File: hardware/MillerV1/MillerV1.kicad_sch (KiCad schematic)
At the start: 281 parts, among them IC1 TUSB1106PWR, J2 Conn_02x04_Counter_Clockwise, Q1 Q12MHz/20pF/10ppm/4P/3.2x2.5mm, U1 CCGM1A1(FBGA-324), U10 RP2040(QFN-56_7x7mm_P0.4mm), U11 TPS62A02ADRLR(SOT-563-6), U12 TPS62A02ADRLR(SOT-563-6), U13 TPS62A02ADRLR(SOT-563-6), U14 TPS62A02ADRLR(SOT-563-6), U15 TPS62A02ADRLR(SOT-563-6)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

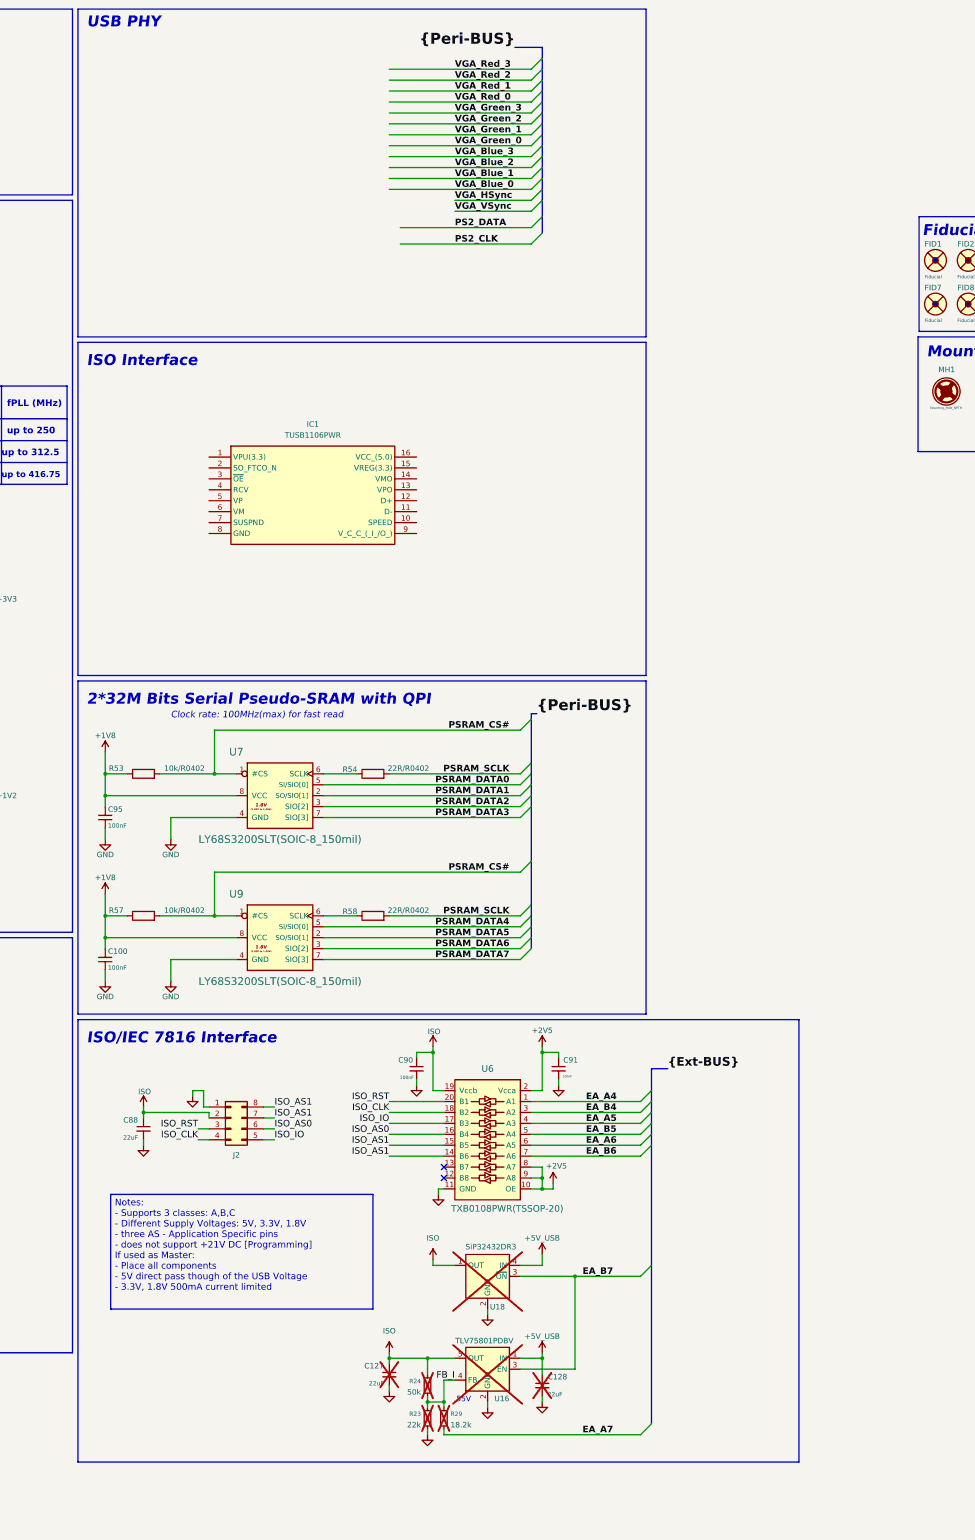
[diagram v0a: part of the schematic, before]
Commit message: merged USB PHY
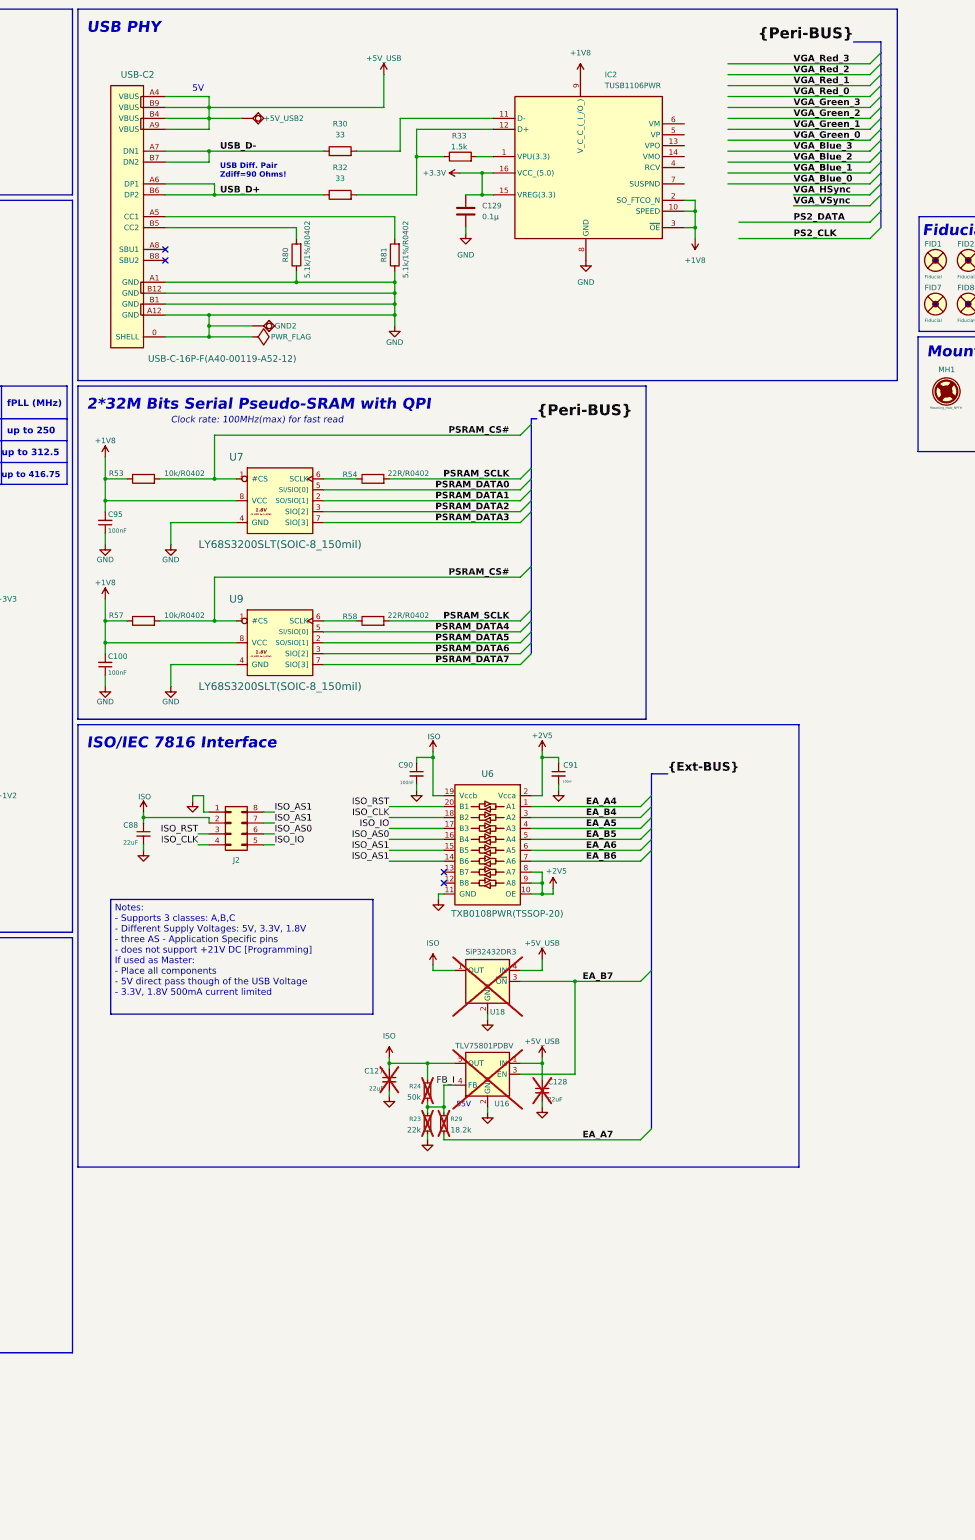
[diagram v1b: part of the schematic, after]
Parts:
- removed IC1: TUSB1106PWR, New_Libary:SOP65P640X120-16N, symbol New_Library:TUSB1106PWR
- added +5V_USB2, GND2: TESTPAD, OLIMEX_Other-FP:TEST_PAD_40x70_Round, symbol OLIMEX_OTHER:TESTPAD
- added C129: 0.1µ, New_Libary:C_0402_5MIL_DWS, symbol Device:C
- added IC2: TUSB1106PWR, New_Libary:SOP65P640X120-16N, symbol New_Library:TUSB1106PWR
- added R30, R32: 33, New_Libary:R_0402_5MIL_DWS, symbol Device:R
- added R33: 1.5k, New_Libary:R_0402_5MIL_DWS, symbol Device:R
- added R80, R81: 5.1k/1%/R0402, OLIMEX_RLC-FP:R_0402_5MIL_DWS, symbol OLIMEX_RCL:R
- added USB-C2: USB-C-16P-F(A40-00119-A52-12), New_Libary:USB2.0_TYPE-C(A40-00119-A52-12)_Paste, symbol OLIMEX_Connectors:USB2.0_TYPE-C(A40-00119-A52-12)
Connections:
- net +1V8: now also IC2.10 (SPEED), IC2.2 (SO_FTCO_N), IC2.3 (~{OE}), IC2.9 (V_C_C_(_I_/O_))
- net +5V_USB: now also +5V_USB2.1 (Pad), USB-C2.A4 (VBUS), USB-C2.A9 (VBUS), USB-C2.B4 (VBUS), USB-C2.B9 (VBUS)
- net GND: now also C129.2, GND2.1 (Pad), IC2.8 (GND), R80.1, R81.1, USB-C2.0 (SHELL), USB-C2.A1 (GND), USB-C2.A12 (GND), USB-C2.B1 (GND), USB-C2.B12 (GND)
- net USB_D+: now also R32.1, USB-C2.A6 (DP1), USB-C2.B6 (DP2)
- net USB_D-: now also R30.1, USB-C2.A7 (DN1), USB-C2.B7 (DN2)
- new net: IC2.12 (D+), R32.2, R33.1
- new net: R81.2, USB-C2.A5 (CC1)
- new net: IC2.1 (VPU(3.3)), R33.2
- new net: IC2.11 (D-), R30.2
- new net: R80.2, USB-C2.B5 (CC2)
- new net +3.3V: C129.1, IC2.15 (VREG(3.3)), IC2.16 (VCC_(5.0))
- no-connect marks 5 -> 7
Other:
- note added: "5V"
- note removed: "ISO Interface"
- moved on the sheet: C100, C127, C128, C88, C90, C91, C95, J2, R23, R24, R29, R53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

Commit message: assigned FPGA pins to USB PHY
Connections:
- net PS2_CLK is gone; now on net SUSPEND: U1.N1 (IO_WB_A0)
- net PS2_DATA is gone; now on net RCV: U1.N2 (IO_WB_B0)
- net VGA_Green_0 is gone; now on net VP: U1.K2 (IO_WB_B5)
- net VGA_Green_1 is gone; now on net VM: U1.K1 (IO_WB_A5)
- net VGA_Red_0 is gone; now on net VMO: U1.L2 (IO_WB_B3)
- net VGA_Red_1 is gone; now on net VPO: U1.L1 (IO_WB_A3)
- net VPO: now reaches IC2.13 (VPO)
- net VMO: now reaches IC2.14 (VMO)
- net RCV: now reaches IC2.4 (RCV)
- net VP: now reaches IC2.5 (VP)
- net VM: now reaches IC2.6 (VM)
- net SUSPEND: now reaches IC2.7 (SUSPND)
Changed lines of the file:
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@@
 	(wire
 		(pts
+			(xy 730.25 52.07) (xy 722.63 52.07)
+		)
+		(stroke
+			(width 0)
+			(type default)
+		)
+	)
+	(wire
+		(pts
 			(xy 588.01 139.7) (xy 588.01 137.16)
 		)
@@
 	(wire
 		(pts
+			(xy 722.63 55.88) (xy 727.71 55.88)
+		)
+		(stroke
+			(width 0)
+			(type default)
+		)
+	)
+	(wire
+		(pts
 			(xy 152.4 292.1) (xy 165.1 292.1)
 		)
@@
 	(wire
 		(pts
+			(xy 723.9 33.02) (xy 723.9 46.99)
+		)
+		(stroke
+			(width 0)
+			(type default)
+		)
+	)
+	(wire
+		(pts
 			(xy 43.18 247.65) (xy 86.36 247.65)
 		)
@@
 	(wire
 		(pts
-			(xy 732.79 35.56) (xy 765.81 35.56)
-		)
-		(stroke
-			(width 0)
-			(type default)
-		)
-	)
-	(wire
-		(pts
 			(xy 439.42 44.45) (xy 436.88 44.45)
 		)
@@
 	(wire
 		(pts
-			(xy 735.33 68.58) (xy 765.81 68.58)
+			(xy 68.58 93.98) (xy 78.74 93.98)
 		)
 		(stroke
@@
 	(wire
 		(pts
-			(xy 68.58 93.98) (xy 78.74 93.98)
+			(xy 154.94 76.2) (xy 167.64 76.2)
 		)
 		(stroke
@@
 	(wire
 		(pts
-			(xy 154.94 76.2) (xy 167.64 76.2)
+			(xy 725.17 35.56) (xy 765.81 35.56)
 		)
 		(stroke
@@
 	(wire
 		(pts
+			(xy 725.17 49.53) (xy 722.63 49.53)
+		)
+		(stroke
+			(width 0)
+			(type default)
+		)
+	)
+	(wire
+		(pts
 			(xy 449.58 251.46) (xy 449.58 254)
 		)
@@
 	(wire
 		(pts
+			(xy 722.63 45.72) (xy 765.81 45.72)
+		)
+		(stroke
+			(width 0)
+			(type default)
+		)
+	)
+	(wire
+		(pts
 			(xy 342.9 147.32) (xy 342.9 152.4)
 		)
@@
 	(wire
 		(pts
+			(xy 730.25 64.77) (xy 765.81 64.77)
+		)
+		(stroke
+			(width 0)
+			(type default)
+		)
+	)
+	(wire
+		(pts
 			(xy 347.98 111.76) (xy 347.98 114.3)
 		)
@@
 		)
 	)
+	(wire
+		(pts
+			(xy 722.63 43.18) (xy 765.81 43.18)
+		)
+		(stroke
+			(width 0)
+			(type default)
+		)
+	)
 	(bus
 		(pts
@@
 	(wire
 		(pts
+			(xy 723.9 46.99) (xy 722.63 46.99)
+		)
+		(stroke
+			(width 0)
+			(type default)
+		)
+	)
+	(wire
+		(pts
 			(xy 431.8 82.55) (xy 431.8 97.79)
 		)
@@
 	(wire
 		(pts
+			(xy 727.71 68.58) (xy 765.81 68.58)
+		)
+		(stroke
+			(width 0)
+			(type default)
+		)
+	)
+	(wire
+		(pts
 			(xy 137.16 327.66) (xy 160.02 327.66)
 		)
@@
 	(wire
 		(pts
+			(xy 722.63 43.18) (xy 722.63 41.91)
+		)
+		(stroke
+			(width 0)
+			(type default)
+		)
+	)
+	(wire
+		(pts
 			(xy 464.82 102.87) (xy 464.82 110.49)
 		)
@@
 	(wire
 		(pts
+			(xy 723.9 33.02) (xy 765.81 33.02)
+		)
+		(stroke
+			(width 0)
+			(type default)
+		)
+	)
+	(wire
+		(pts
 			(xy 347.98 114.3) (xy 347.98 116.84)
 		)
@@
 		)
 	)
+	(wire
+		(pts
+			(xy 725.17 35.56) (xy 725.17 49.53)
+		)
+		(stroke
+			(width 0)
+			(type default)
+		)
+	)
 	(bus
 		(pts
@@
 	(wire
 		(pts
+			(xy 727.71 68.58) (xy 727.71 55.88)
+		)
+		(stroke
+			(width 0)
+			(type default)
+		)
+	)
+	(wire
+		(pts
 			(xy 367.03 370.84) (xy 382.27 370.84)
 		)
@@
 	(wire
 		(pts
-			(xy 732.79 45.72) (xy 765.81 45.72)
-		)
-		(stroke
-			(width 0)
-			(type default)
-		)
-	)
-	(wire
-		(pts
 			(xy 457.2 110.49) (xy 457.2 118.11)
 		)
@@
 		)
 	)
-	(wire
-		(pts
-			(xy 732.79 43.18) (xy 765.81 43.18)
-		)
-		(stroke
-			(width 0)
-			(type default)
-		)
-	)
 	(bus
 		(pts
@@
 	(wire
 		(pts
+			(xy 730.25 64.77) (xy 730.25 52.07)
+		)
+		(stroke
+			(width 0)
+			(type default)
+		)
+	)
+	(wire
+		(pts
 			(xy 147.32 358.14) (xy 142.24 358.14)
 		)
@@
 	(wire
 		(pts
-			(xy 735.33 64.77) (xy 765.81 64.77)
-		)
-		(stroke
-			(width 0)
-			(type default)
-		)
-	)
-	(wire
-		(pts
 			(xy 347.98 119.38) (xy 347.98 121.92)
 		)
@@
 	(wire
 		(pts
-			(xy 732.79 33.02) (xy 765.81 33.02)
-		)
-		(stroke
-			(width 0)
-			(type default)
-		)
-	)
-	(wire
-		(pts
 			(xy 398.78 99.06) (xy 398.78 101.6)
 		)
@@
 	(wire
 		(pts
+			(xy 722.63 45.72) (xy 722.63 44.45)
+		)
+		(stroke
+			(width 0)
+			(type default)
+		)
+	)
+	(wire
+		(pts
 			(xy 378.46 104.14) (xy 378.46 106.68)
 		)
@@
 		)
 	)
-	(label "VGA_Green_0"
+	(label "VP"
 		(at 748.03 45.72 0)
 		(effects
@@
 		)
 	)
-	(label "VGA_Red_0"
+	(label "VMO"
 		(at 226.06 78.74 0)
 		(effects
@@
 		)
 	)
-	(label "PS2_DATA"
+	(label "RCV"
 		(at 748.03 64.77 0)
 		(effects
@@
 		)
 	)
-	(label "VGA_Red_1"
+	(label "VPO"
 		(at 748.03 33.02 0)
 		(effects
@@
 		)
 	)
-	(label "VGA_Red_1"
+	(label "VPO"
 		(at 226.06 76.2 0)
 		(effects
@@
 		)
 	)
-	(label "PS2_DATA"
+	(label "RCV"
 		(at 226.06 63.5 0)
 		(effects
@@
 		)
 	)
-	(label "VGA_Green_1"
+	(label "VM"
 		(at 748.03 43.18 0)
 		(effects
@@
 		)
 	)
-	(label "PS2_CLK"
+	(label "SUSPEND"
 		(at 226.06 60.96 0)
 		(effects
@@
 		)
 	)
-	(label "VGA_Red_0"
+	(label "VMO"
 		(at 748.03 35.56 0)
 		(effects
@@
 		)
 	)
-	(label "VGA_Green_0"
+	(label "VP"
 		(at 226.06 91.44 0)
 		(effects
@@
 		)
 	)
-	(label "PS2_CLK"
+	(label "SUSPEND"
 		(at 748.03 68.58 0)
 		(effects
@@
 		)
 	)
-	(label "VGA_Green_1"
+	(label "VM"
 		(at 226.06 88.9 0)
 		(effects

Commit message: Alles Kapput mach das neu in MAIN
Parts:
- removed IC2: TUSB1106PWR, New_Libary:SOP65P640X120-16N, symbol New_Library:TUSB1106PWR
- added C130, C131: 0.1µ, New_Libary:C_0402_5MIL_DWS, symbol Device:C
- added IC1: TUSB1106PWR, New_Libary:SOP65P640X120-16N, symbol New_Library:TUSB1106PWR
- added JP1: Jumper_3_Open, Connector_PinHeader_2.54mm:PinHeader_1x03_P2.54mm_Vertical, symbol Jumper:Jumper_3_Open
- added R34: 1.5k, New_Libary:R_0402_5MIL_DWS, symbol Device:R
- added R35: 10k, New_Libary:R_0402_5MIL_DWS, symbol Device:R
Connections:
- net +1V8: now also C131.1, IC1.9 (V_C_C_(_I_/O_)), JP1.1 (A), R35.1
- net +3.3V: now also C130.1, IC1.15 (VREG(3.3)), IC1.16 (VCC_(5.0)); no longer C129.1
- net +5V_USB: now also C129.1
- net GND: now also C130.2, C131.2, IC1.8 (GND)
- net USB_D+: no longer R32.1, USB-C2.A6 (DP1), USB-C2.B6 (DP2)
- net USB_D-: no longer R30.1, USB-C2.A7 (DN1), USB-C2.B7 (DN2)
- net VGA_Green_2: now also IC1.4 (RCV)
- net VGA_Green_3: now also IC1.14 (VMO)
- net VGA_Red_2: now also IC1.6 (VM)
- net VGA_Red_3: now also JP1.3 (B)
- net at R32.2: now also IC1.12 (D+), R34.1; no longer R33.1
- net at R33.2: now also IC1.1 (VPU(3.3)), R34.2
- net at R30.2: now also R33.1, IC1.11 (D-)
- new net: IC1.3 (~{OE}), JP1.2 (C)
- new net USB_2_D+: R32.1, USB-C2.A6 (DP1), USB-C2.B6 (DP2)
- new net USB_2_D-: R30.1, USB-C2.A7 (DN1), USB-C2.B7 (DN2)
- new net VGA_Green_0: IC1.10 (SPEED), R35.2
- new net VGA_Green_1: IC1.7 (SUSPND)
- new net VGA_Red_0: IC1.13 (VPO)
- new net VGA_Red_1: IC1.5 (VP)
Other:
- moved on the sheet: FID1, FID10, FID11, FID12, FID2, FID3, FID4, FID5, FID6, FID7, FID8, FID9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

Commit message: kleine Änderungen und GND
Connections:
- net VGA_Blue_0: now also JP1.3 (B)
- net VGA_Red_3: no longer JP1.3 (B)
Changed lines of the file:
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@@
 	(wire
 		(pts
-			(xy 717.55 24.13) (xy 744.22 24.13)
-		)
-		(stroke
-			(width 0)
-			(type default)
-		)
-	)
-	(wire
-		(pts
 			(xy 193.04 40.64) (xy 193.04 43.18)
 		)
@@
 	(wire
 		(pts
-			(xy 744.22 24.13) (xy 744.22 30.48)
-		)
-		(stroke
-			(width 0)
-			(type default)
-		)
-	)
-	(wire
-		(pts
 			(xy 312.42 76.2) (xy 304.8 76.2)
 		)
@@
 				(thickness 0.3048)
 				(bold yes)
+			)
+			(justify left bottom)
+		)
+	)
+	(label "VGA_Blue_0"
+		(at 717.55 24.13 0)
+		(effects
+			(font
+				(size 0.762 0.762)
+				(thickness 0.3048)
+				(bold yes)

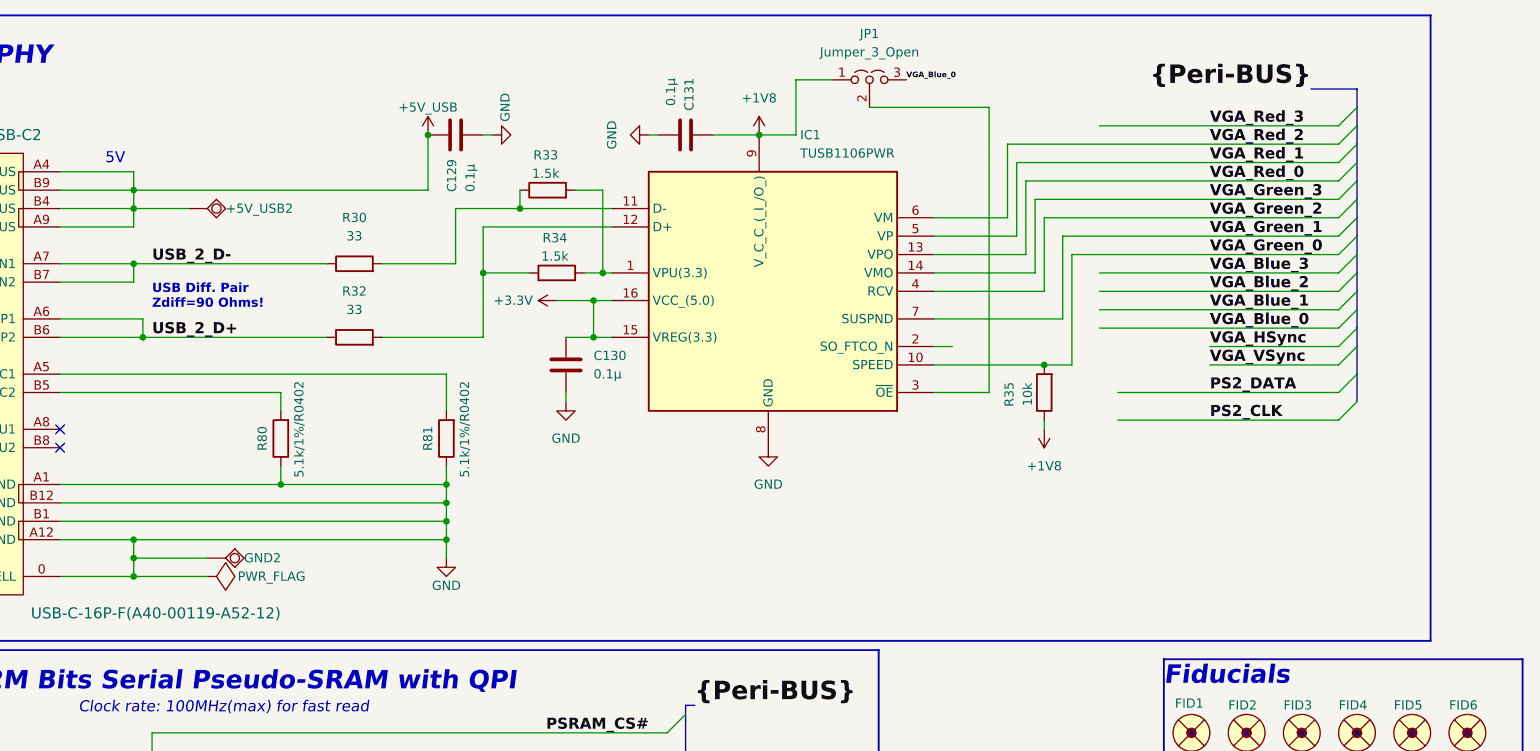
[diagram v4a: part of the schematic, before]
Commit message: fixed scematic/pcb differences
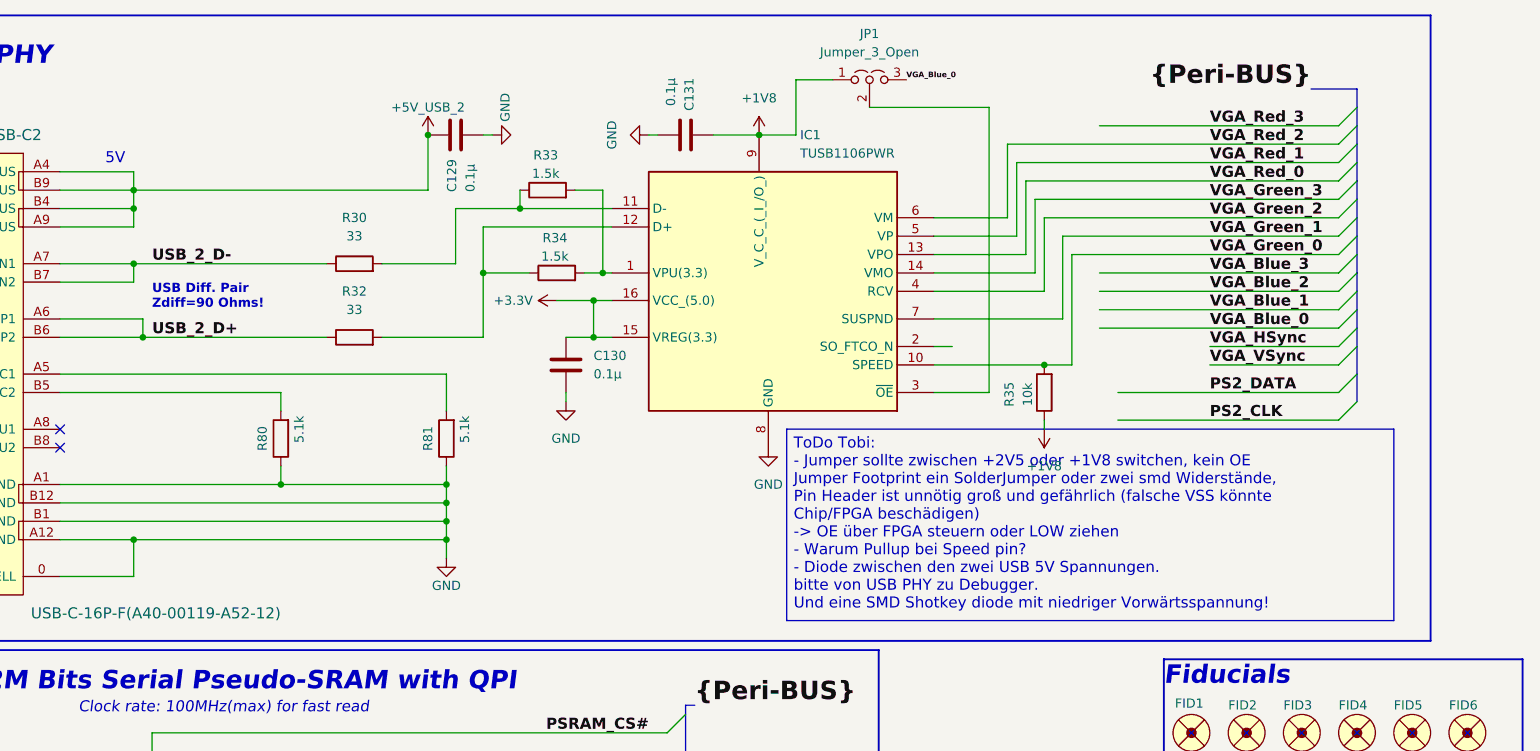
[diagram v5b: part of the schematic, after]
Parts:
- removed +5V_USB2, GND2: TESTPAD, OLIMEX_Other-FP:TEST_PAD_40x70_Round, symbol OLIMEX_OTHER:TESTPAD
- R80, R81: value 5.1k/1%/R0402 -> 5.1k; footprint OLIMEX_RLC-FP:R_0402_5MIL_DWS -> Resistor_SMD:R_0402_1005Metric_Pad0.72x0.64mm_HandSolder
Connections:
- net +5V_USB: no longer C129.1, USB-C2.A4 (VBUS), USB-C2.A9 (VBUS), USB-C2.B4 (VBUS), USB-C2.B9 (VBUS)
- new net +5V_USB_2: C129.1, USB-C2.A4 (VBUS), USB-C2.A9 (VBUS), USB-C2.B4 (VBUS), USB-C2.B9 (VBUS)
